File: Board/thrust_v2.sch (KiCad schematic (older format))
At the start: 187 parts, among them J1 Conn_01x05, J10 BattVolt, J12 MX-67068-9000(USB-B), J13 Conn_SWD, J14 Motor, J15 BattCurr, J16 SensorRPM, J17 UART/I2C, J2 Conn_01x05, J3 Conn_01x05, J4 Conn_3.3V, J5 Conn_3.3VA, J7 Conn_01x05, J8 Ext_5V, M1 Mounting_Hole, M2 Mounting_Hole, M3 Mounting_Hole, M4 Mounting_Hole, Q1 MMBT4403, Q2 MMBT4403, Q3 MMBT4403, SW2 BootBtn, SW4 UserBtn, SW5 ResetBtn, U1 NCP1117-3.3/LDI1117-3.3H, U12 STM32F401RETx, U2 MIC5504-3.3YM5, U3 HX711, U4 HX711, U5 HX711, U6 USBLC6-2P6, U7 MCP1501_SOT23, U8 LCD_SSD1306_I2C, Y1 8MHz, Y2 32.768kHz

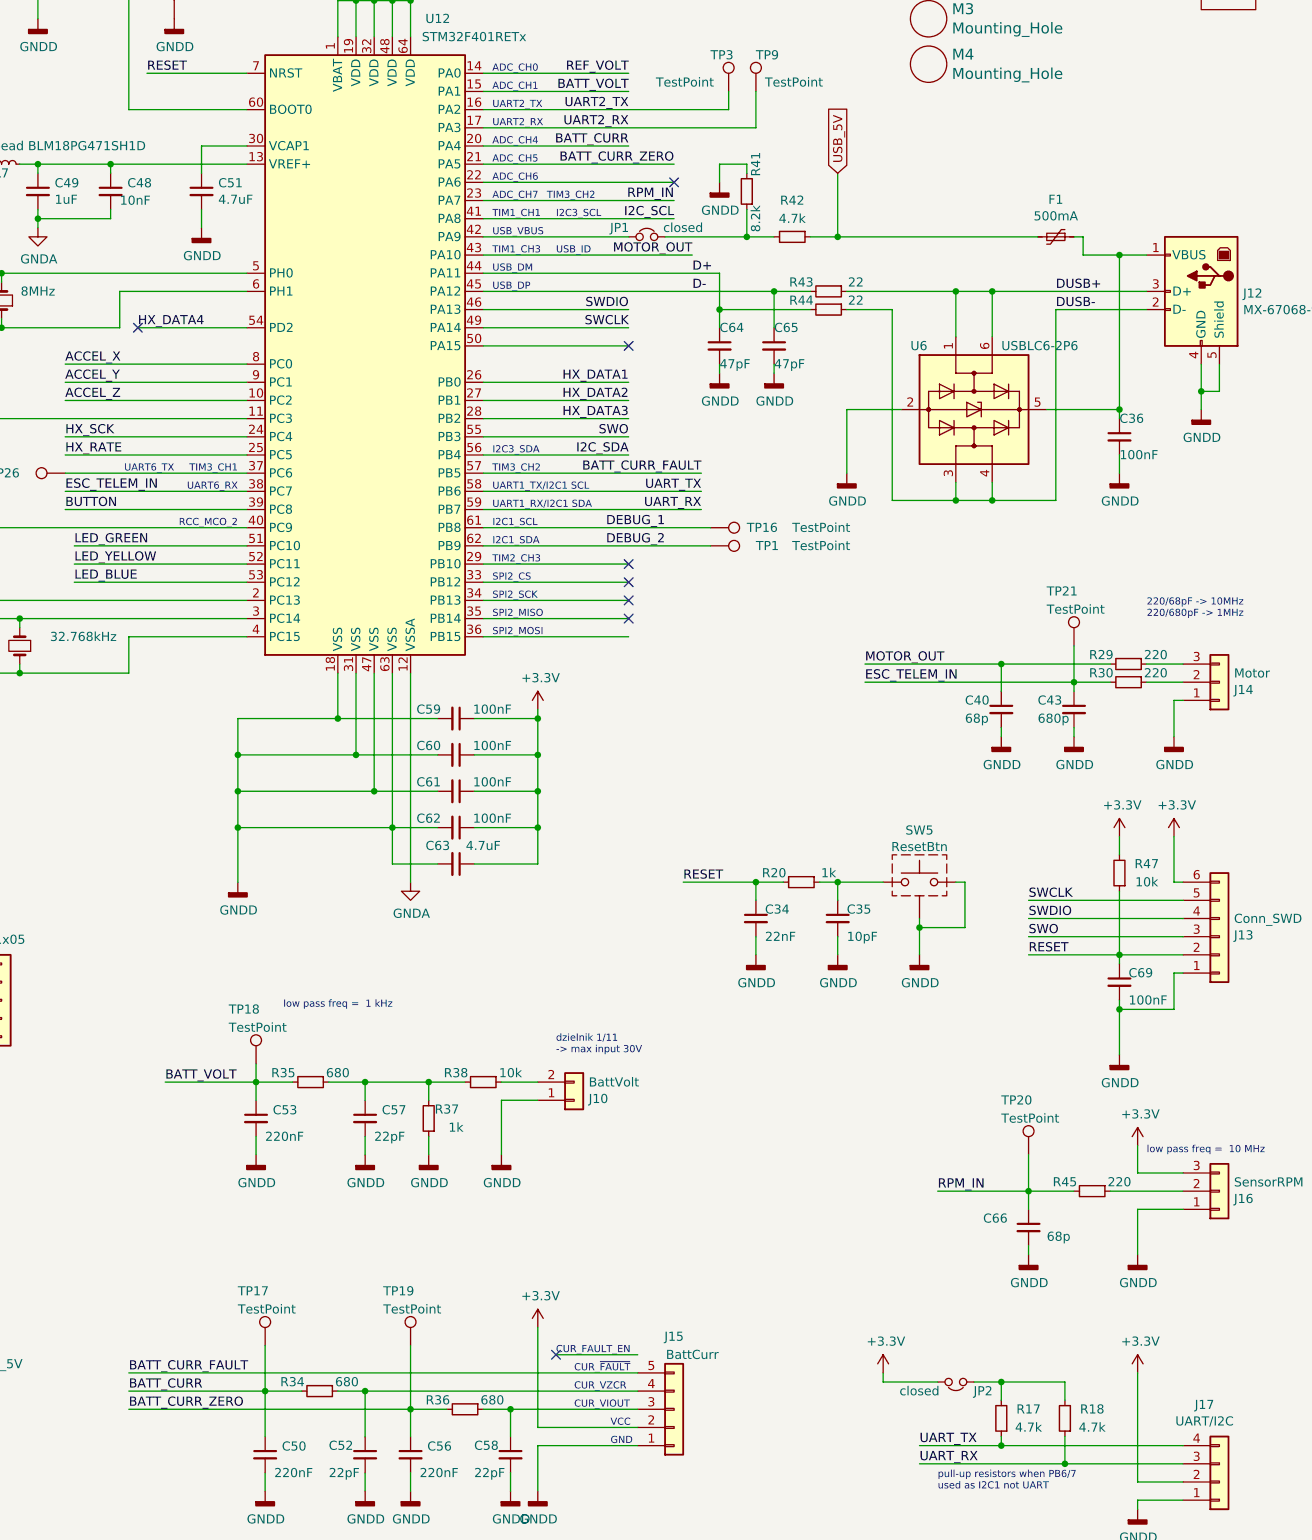
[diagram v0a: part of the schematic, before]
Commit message: fix curr_zero connection
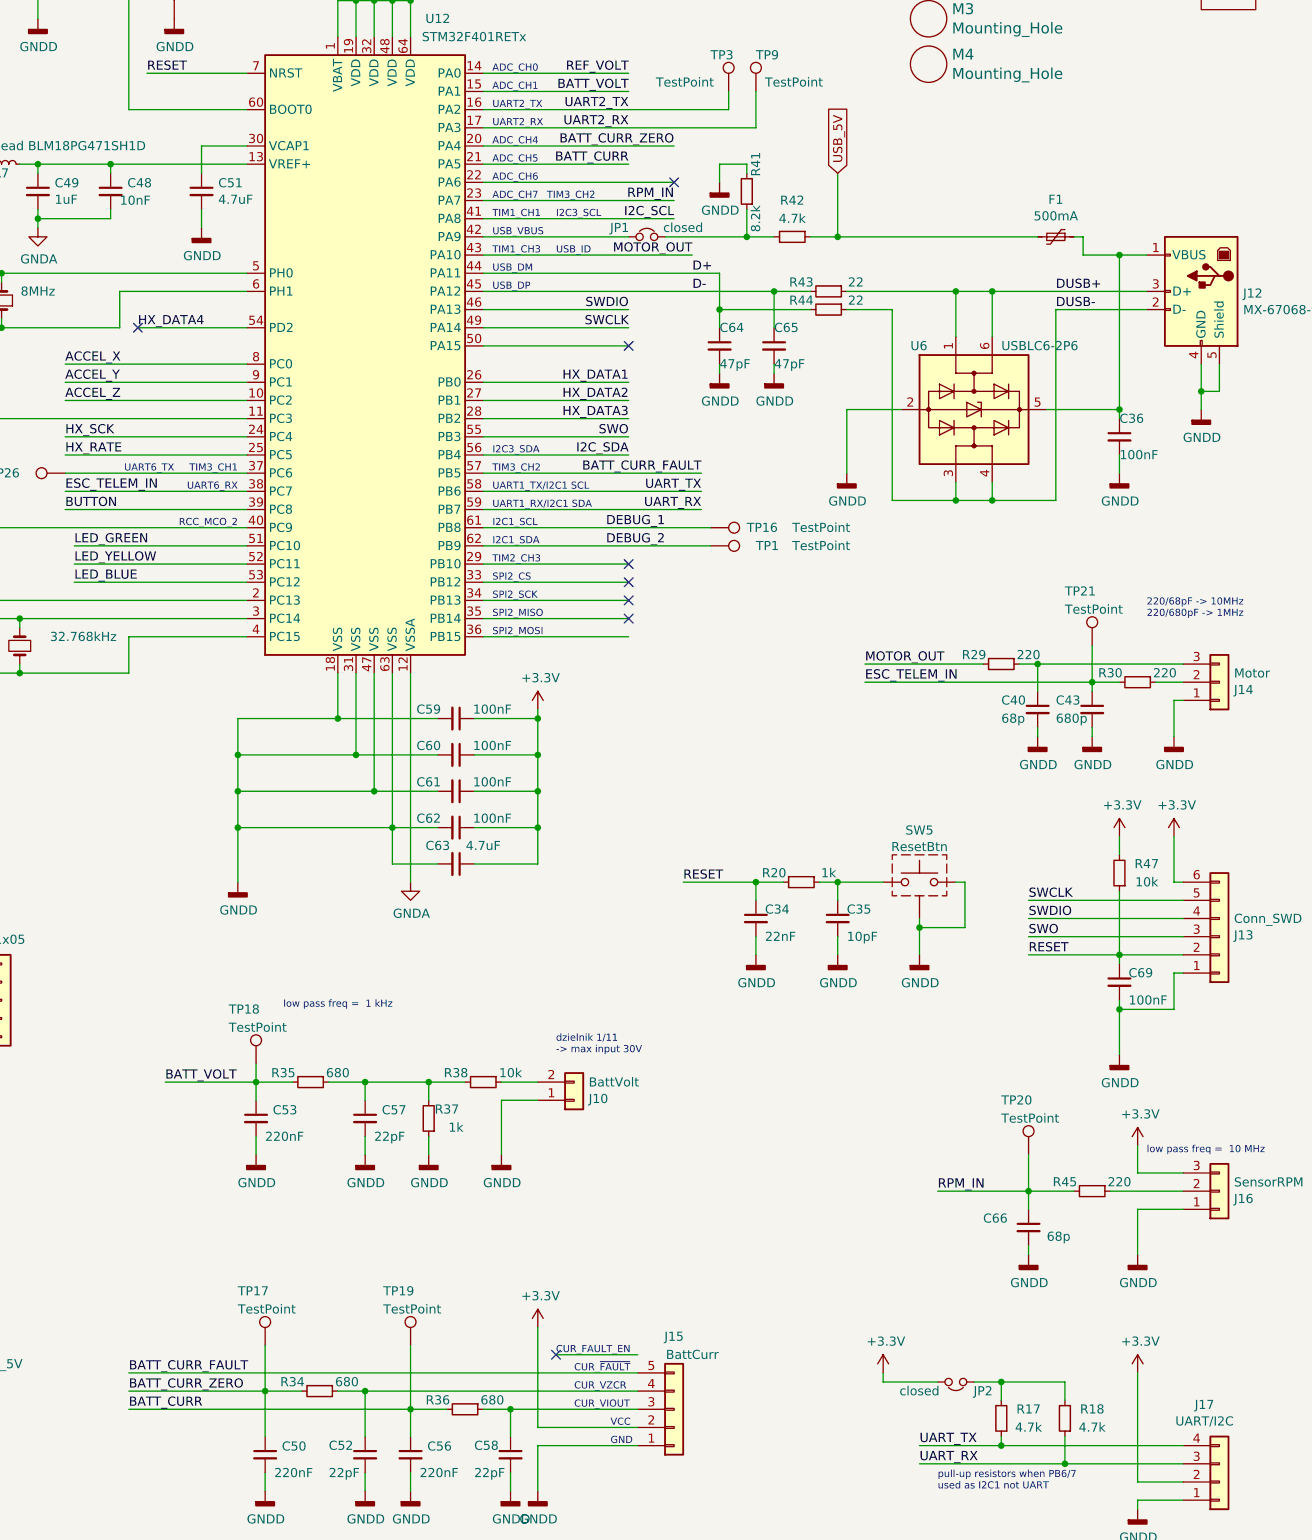
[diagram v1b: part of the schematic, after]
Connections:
- net BATT_CURR: now also C56.1, R36.2, TP19.1, U12.21 (PA5); no longer C50.1, R34.2, TP17.1, U12.20 (PA4)
- net BATT_CURR_ZERO: now also C50.1, R34.2, TP17.1, U12.20 (PA4); no longer C56.1, R36.2, TP19.1, U12.21 (PA5)
- net MOTOR_OUT: no longer C40.1
- net at J14.3 (Pin_3), R29.1: now also C40.1
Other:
- moved on the sheet: C40, C43, R29, R30, TP21
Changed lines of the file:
@@
 Wire Wire Line
 	11700 8950 12250 8950
+Text Label 9450 8850 0    50   ~ 0
+BATT_CURR
 Text Label 9450 8750 0    50   ~ 0
-BATT_CURR
-Text Label 9450 8850 0    50   ~ 0
 BATT_CURR_ZERO
 Text Label 9450 8650 0    50   ~ 0
@@
 L Connector:TestPoint TP21
 U 1 1 63B43829
-P 14650 4650
-F 0 "TP21" H 14500 4950 50  0000 L CNN
-F 1 "TestPoint" H 14500 4850 50  0000 L CNN
-F 2 "TestPoint:TestPoint_Pad_1.5x1.5mm" H 14850 4650 50  0001 C CNN
-F 3 "~" H 14850 4650 50  0001 C CNN
-	1    14650 4650
+P 14750 4650
+F 0 "TP21" H 14600 4950 50  0000 L CNN
+F 1 "TestPoint" H 14600 4850 50  0000 L CNN
+F 2 "TestPoint:TestPoint_Pad_1.5x1.5mm" H 14950 4650 50  0001 C CNN
+F 3 "~" H 14950 4650 50  0001 C CNN
+	1    14750 4650
 	1    0    0    -1
 $EndComp
@@
 F 3 "" H 15200 5150 50  0001 C CNN
 	1    15200 5150
-	1    0    0    -1
-$EndComp
-$Comp
-L power:GNDD #PWR0138
-U 1 1 61BD411F
-P 14650 5150
-F 0 "#PWR0138" H 14650 4900 50  0001 C CNN
-F 1 "GNDD" H 14654 4995 50  0000 C CNN
-F 2 "" H 14650 5150 50  0001 C CNN
-F 3 "" H 14650 5150 50  0001 C CNN
-	1    14650 5150
 	1    0    0    -1
 $EndComp
@@
 Text Notes 11450 4400 0    39   ~ 0
 SPI2_SCK
-Wire Wire Line
-	11400 2000 12450 2000
 NoConn ~ 9500 2900
 Text Notes 10050 4000 2    39   ~ 0
@@
 Text Label 9100 3800 0    51   ~ 0
 ESC_TELEM_IN
-Text Label 12450 2000 2    50   ~ 0
+Text Label 12450 1900 2    50   ~ 0
 BATT_CURR_ZERO
-Text Label 12200 1900 2    50   ~ 0
+Text Label 12200 2000 2    50   ~ 0
 BATT_CURR
 Text Label 12600 3700 2    50   ~ 0
@@
 Wire Wire Line
 	11400 2400 12200 2400
-Wire Wire Line
-	11400 1900 12200 1900
 Wire Wire Line
 	11400 1600 12200 1600
@@
 Wire Wire Line
 	8500 10000 9200 10000
-$Comp
-L Device:R_Small R30
-U 1 1 60A51BFB
-P 14950 4850
-F 0 "R30" V 14900 4700 50  0000 C CNN
-F 1 "220" V 14900 5000 50  0000 C CNN
-F 2 "Resistor_SMD:R_0603_1608Metric_Pad0.98x0.95mm_HandSolder" H 14950 4850 50  0001 C CNN
-F 3 "~" H 14950 4850 50  0001 C CNN
-	1    14950 4850
-	0    1    1    0
-$EndComp
-$Comp
-L Device:C_Small C43
-U 1 1 60A523A6
-P 14650 5000
-F 0 "C43" H 14450 5050 50  0000 L CNN
-F 1 "680p" H 14450 4950 50  0000 L CNN
-F 2 "Capacitor_SMD:C_0603_1608Metric_Pad1.08x0.95mm_HandSolder" H 14650 5000 50  0001 C CNN
-F 3 "~" H 14650 5000 50  0001 C CNN
-	1    14650 5000
-	1    0    0    -1
-$EndComp
-$Comp
-L Device:C_Small C40
-U 1 1 60A529E7
-P 14250 5000
-F 0 "C40" H 14050 5050 50  0000 L CNN
-F 1 "68p" H 14050 4950 50  0000 L CNN
-F 2 "Capacitor_SMD:C_0603_1608Metric_Pad1.08x0.95mm_HandSolder" H 14250 5000 50  0001 C CNN
-F 3 "~" H 14250 5000 50  0001 C CNN
-	1    14250 5000
-	1    0    0    -1
-$EndComp
-$Comp
-L Device:R_Small R29
-U 1 1 60A52D27
-P 14950 4750
-F 0 "R29" V 14900 4600 50  0000 C CNN
-F 1 "220" V 14900 4900 50  0000 C CNN
-F 2 "Resistor_SMD:R_0603_1608Metric_Pad0.98x0.95mm_HandSolder" H 14950 4750 50  0001 C CNN
-F 3 "~" H 14950 4750 50  0001 C CNN
-	1    14950 4750
-	0    1    1    0
-$EndComp
-Wire Wire Line
-	15050 4750 15250 4750
-Wire Wire Line
-	15050 4850 15250 4850
-$Comp
-L power:GNDD #PWR0151
-U 1 1 60E2B20A
-P 14250 5150
-F 0 "#PWR0151" H 14250 4900 50  0001 C CNN
-F 1 "GNDD" H 14254 4995 50  0000 C CNN
-F 2 "" H 14250 5150 50  0001 C CNN
-F 3 "" H 14250 5150 50  0001 C CNN
-	1    14250 5150
-	1    0    0    -1
-$EndComp
-Wire Wire Line
-	14650 5100 14650 5150
-Wire Wire Line
-	14250 5100 14250 5150
-Wire Wire Line
-	14650 4900 14650 4850
-Wire Wire Line
-	14650 4850 14850 4850
-Wire Wire Line
-	14250 4900 14250 4750
-Wire Wire Line
-	14250 4750 14850 4750
-Wire Wire Line
-	13500 4850 14650 4850
-Connection ~ 14650 4850
-Wire Wire Line
-	13500 4750 14250 4750
-Connection ~ 14250 4750
-Wire Wire Line
-	14650 4650 14650 4850
+Wire Wire Line
+	14450 5100 14450 5150
+Wire Wire Line
+	14450 4900 14450 4750
+Wire Wire Line
+	13500 4750 14150 4750
+Connection ~ 14450 4750
 Text Notes 15050 4500 0    39   ~ 0
 220/68pF -> 10MHz\n220/680pF -> 1MHz
@@
 	0    -1   1    0
 $EndComp
+Wire Wire Line
+	15100 4850 15250 4850
+$Comp
+L Device:R_Small R30
+U 1 1 60A51BFB
+P 15000 4850
+F 0 "R30" V 14950 4700 50  0000 C CNN
+F 1 "220" V 14950 5000 50  0000 C CNN
+F 2 "Resistor_SMD:R_0603_1608Metric_Pad0.98x0.95mm_HandSolder" H 15000 4850 50  0001 C CNN
+F 3 "~" H 15000 4850 50  0001 C CNN
+	1    15000 4850
+	0    1    1    0
+$EndComp
+$Comp
+L power:GNDD #PWR0151
+U 1 1 60E2B20A
+P 14450 5150
+F 0 "#PWR0151" H 14450 4900 50  0001 C CNN
+F 1 "GNDD" H 14454 4995 50  0000 C CNN
+F 2 "" H 14450 5150 50  0001 C CNN
+F 3 "" H 14450 5150 50  0001 C CNN
+	1    14450 5150
+	1    0    0    -1
+$EndComp
+$Comp
+L power:GNDD #PWR0138
+U 1 1 61BD411F
+P 14750 5150
+F 0 "#PWR0138" H 14750 4900 50  0001 C CNN
+F 1 "GNDD" H 14754 4995 50  0000 C CNN
+F 2 "" H 14750 5150 50  0001 C CNN
+F 3 "" H 14750 5150 50  0001 C CNN
+	1    14750 5150
+	1    0    0    -1
+$EndComp
+Wire Wire Line
+	14750 5100 14750 5150
+$Comp
+L Device:C_Small C43
+U 1 1 60A523A6
+P 14750 5000
+F 0 "C43" H 14550 5050 50  0000 L CNN
+F 1 "680p" H 14550 4950 50  0000 L CNN
+F 2 "Capacitor_SMD:C_0603_1608Metric_Pad1.08x0.95mm_HandSolder" H 14750 5000 50  0001 C CNN
+F 3 "~" H 14750 5000 50  0001 C CNN
+	1    14750 5000
+	1    0    0    -1
+$EndComp
+Wire Wire Line
+	14750 4650 14750 4850
+Connection ~ 14750 4850
+Wire Wire Line
+	13500 4850 14750 4850
+Wire Wire Line
+	14750 4850 14900 4850
+Wire Wire Line
+	14750 4900 14750 4850
+$Comp
+L Device:C_Small C40
+U 1 1 60A529E7
+P 14450 5000
+F 0 "C40" H 14250 5050 50  0000 L CNN
+F 1 "68p" H 14250 4950 50  0000 L CNN
+F 2 "Capacitor_SMD:C_0603_1608Metric_Pad1.08x0.95mm_HandSolder" H 14450 5000 50  0001 C CNN
+F 3 "~" H 14450 5000 50  0001 C CNN
+	1    14450 5000
+	1    0    0    -1
+$EndComp
+$Comp
+L Device:R_Small R29
+U 1 1 60A52D27
+P 14250 4750
+F 0 "R29" V 14200 4600 50  0000 C CNN
+F 1 "220" V 14200 4900 50  0000 C CNN
+F 2 "Resistor_SMD:R_0603_1608Metric_Pad0.98x0.95mm_HandSolder" H 14250 4750 50  0001 C CNN
+F 3 "~" H 14250 4750 50  0001 C CNN
+	1    14250 4750
+	0    1    1    0
+$EndComp
+Wire Wire Line
+	14350 4750 14450 4750
+Wire Wire Line
+	14450 4750 15250 4750
+Wire Wire Line
+	11400 1900 12450 1900
+Wire Wire Line
+	11400 2000 12200 2000
 $EndSCHEMATC

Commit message: board schematic updated
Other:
- note added: "ADC_CH10"
- note added: "ADC_CH11"
- note added: "ADC_CH12"
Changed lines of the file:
@@
 Wire Wire Line
 	11400 2000 12200 2000
+Text Notes 10050 3100 2    39   ~ 0
+ADC_CH10
+Text Notes 10050 3200 2    39   ~ 0
+ADC_CH11
+Text Notes 10050 3300 2    39   ~ 0
+ADC_CH12
 $EndSCHEMATC
